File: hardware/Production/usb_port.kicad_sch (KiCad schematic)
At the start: 100 parts, among them J401 TYPE-C 16PCB1.6 IP68, Q401 SiZ240DT, Q402 SiZ240DT, Q409 AO3400A, U401 TPS25751DREFR, U402 M24512-DFMC6TG, U403 BQ25756RRVR, U404 TPS62933DRLR, U405 TPD6S300RUKR, U406 TPS7A4101DGNR

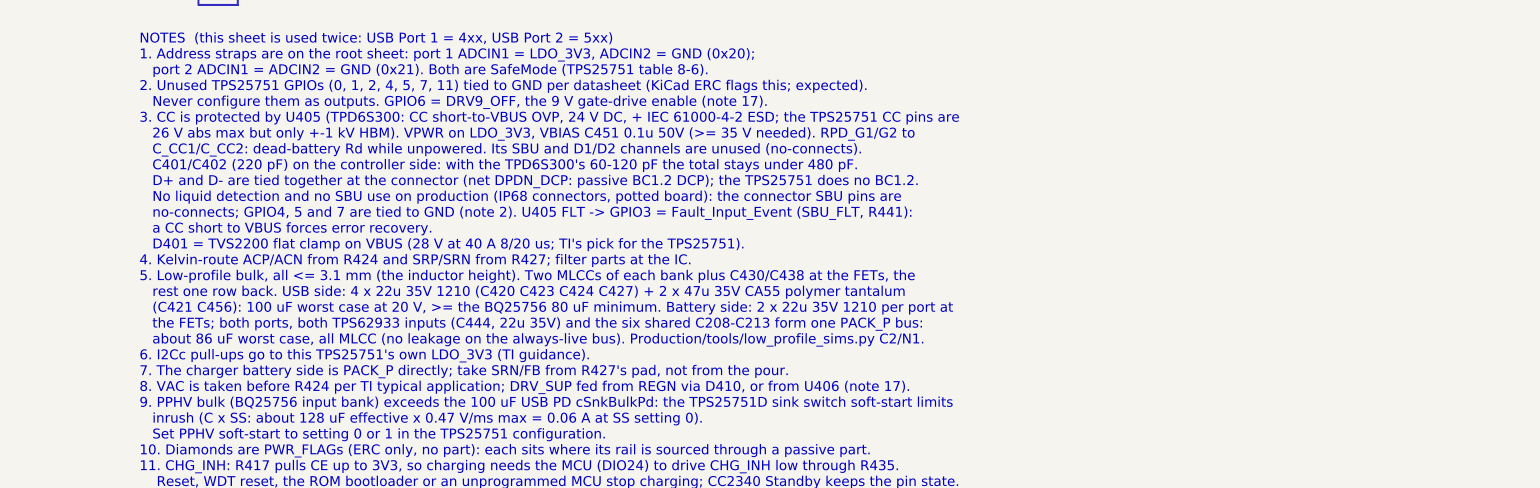
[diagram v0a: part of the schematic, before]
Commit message: Swap D401/D501 TVS2200 to Wuxi Maxinmicro TVS2200DRVR (C55616459)
TI TVS2200DRVR (C523793) was short at JLC for the full order. The
Maxinmicro part has the same pinout (1-3 + EP GND, 4-6 VIN) and the
same 2x2 DFN-6 body (EP 0.9 x 1.7, inside TI's 1.0 x 1.6 +-0.1), and
equal or better headline ratings on its sheet. Footprint unchanged.

- usb_port.kicad_sch: LCSC, Datasheet, Description, Notes and sheet note 3
- jlc BOMs: C523793 -> C55616459
- ordering tracker B04 + README regenerated
- datasheets: add maxinmicro-tvs2200drvr.pdf, index and sources rows

Co-Authored-By: Claude Opus 5.5 <noreply@anthropic.com>
Claude-Session: https://claude.ai/code/session_01LzE9uxXbYduMoWapuqEHhW
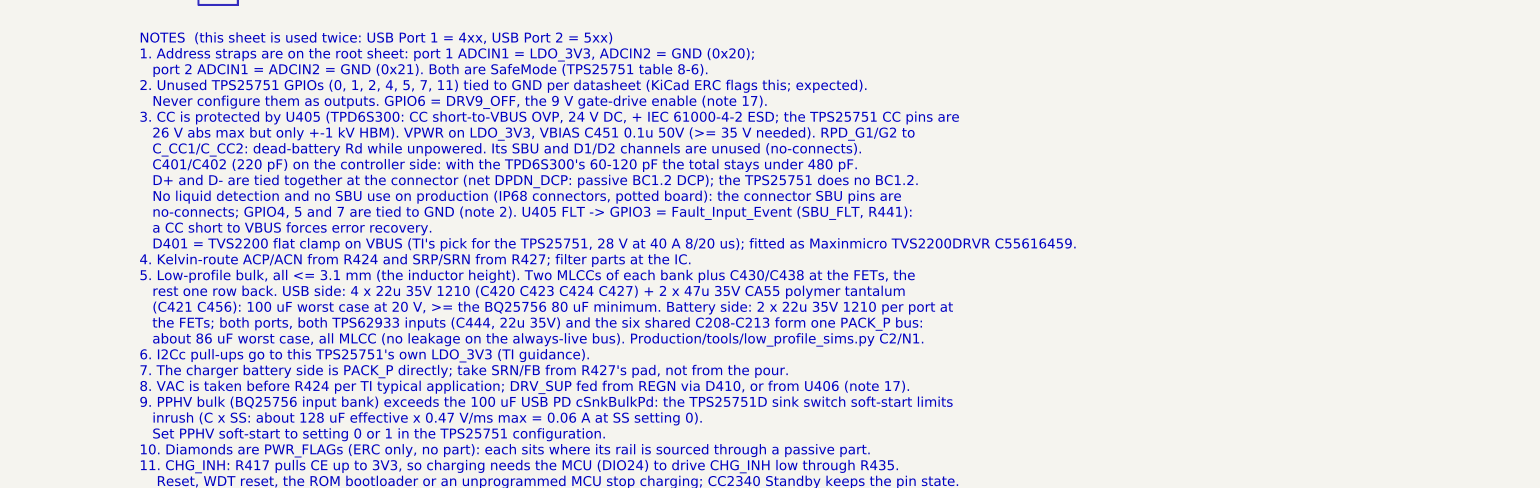
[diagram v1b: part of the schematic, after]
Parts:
- D401: LCSC C523793 -> C55616459; Notes VBUS flat-clamp TVS (TI's recommendation for the TPS25751; 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 -> VBUS flat-clamp TVS. Fitted part: Wuxi Maxinmicro TVS2200DR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

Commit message: C421/C456/C521/C556: KEMET T593V686M035APE070 replaces CCTC CA55-D035M476T
68 uF 35 V polymer tantalum, 70 mOhm, 7343-20 (2.0 mm) on the same D land
pattern, so no footprint or board change. Schematic fields and notes 5/9,
generators, JLC BOMs, tracker L02, low_profile_sims option C4 (133 uF worst
case at 20 V, 20.9 dB damping), 3D model mapping.

Co-Authored-By: Claude Opus 5.5 <noreply@anthropic.com>
Claude-Session: https://claude.ai/code/session_01LzE9uxaEo38wom8h1dA3Sn
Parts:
- C421: value 47u 35V -> 68u 35V; LCSC C2761440 -> (none); MPN CCTC CA55-D035M476T (polymer tantalum) -> KEMET T593V686M035APE070 (polymer tantalum); Notes USB-side bulk with C456 (two 47 uF 35 V polymer tantalum, 1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 -> USB-side bulk with C456 (two KEMET T593V 68 uF 35 V polymer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
- C456: value 47u 35V -> 68u 35V; LCSC C2761440 -> (none); MPN CCTC CA55-D035M476T (polymer tantalum) -> KEMET T593V686M035APE070 (polymer tantalum); Notes Second CA55 47u on AC_SNS_N, see C421 -> Second T593V 68u on AC_SNS_N, see C421
